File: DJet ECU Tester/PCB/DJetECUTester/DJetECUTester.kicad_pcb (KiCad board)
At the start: 2 copper layers, 93 x 79 mm, 103 parts, among them J1 ISP, J10 ECU3, J2 ECU1, J3 USB_B_Mini, J4 BREAKOUT, J5 12V IN, J6 MPS, J7 VAC, J8 INJECTORS, J9 ECU2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

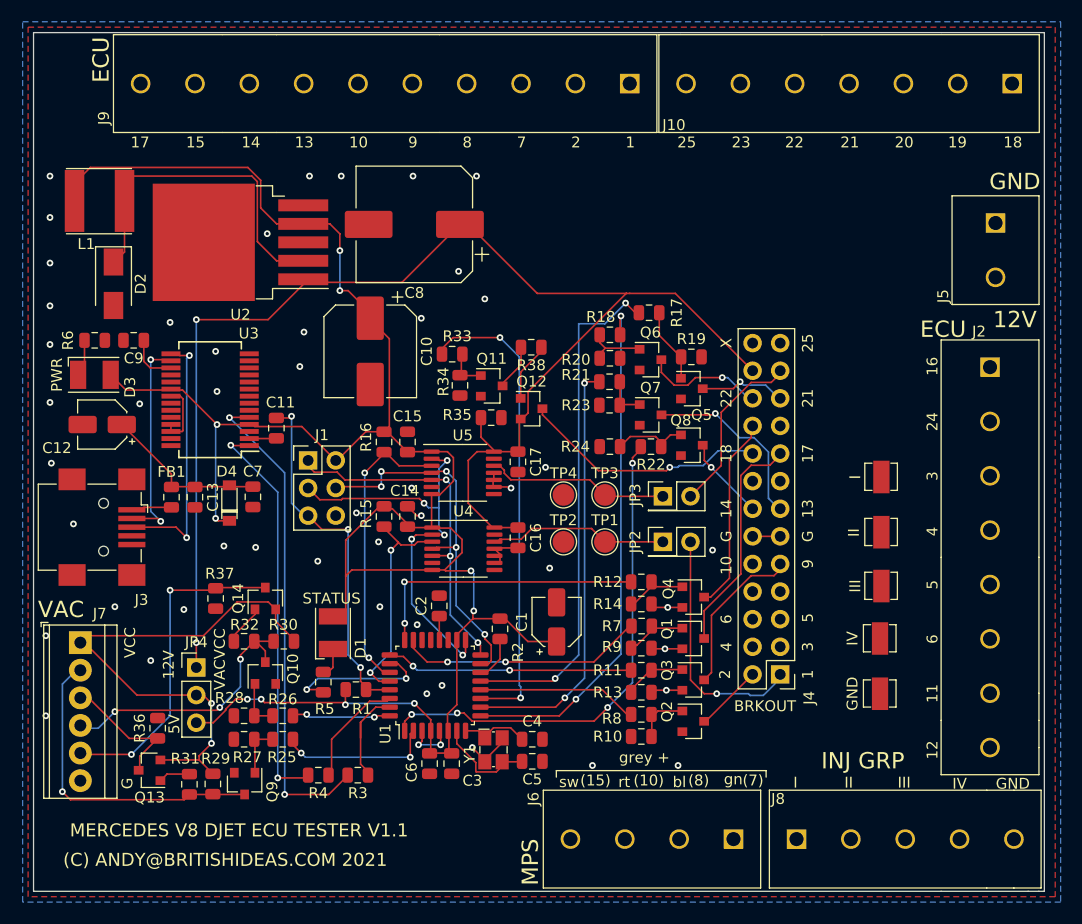
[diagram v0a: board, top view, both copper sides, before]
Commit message: Completed first attempt at new layout.
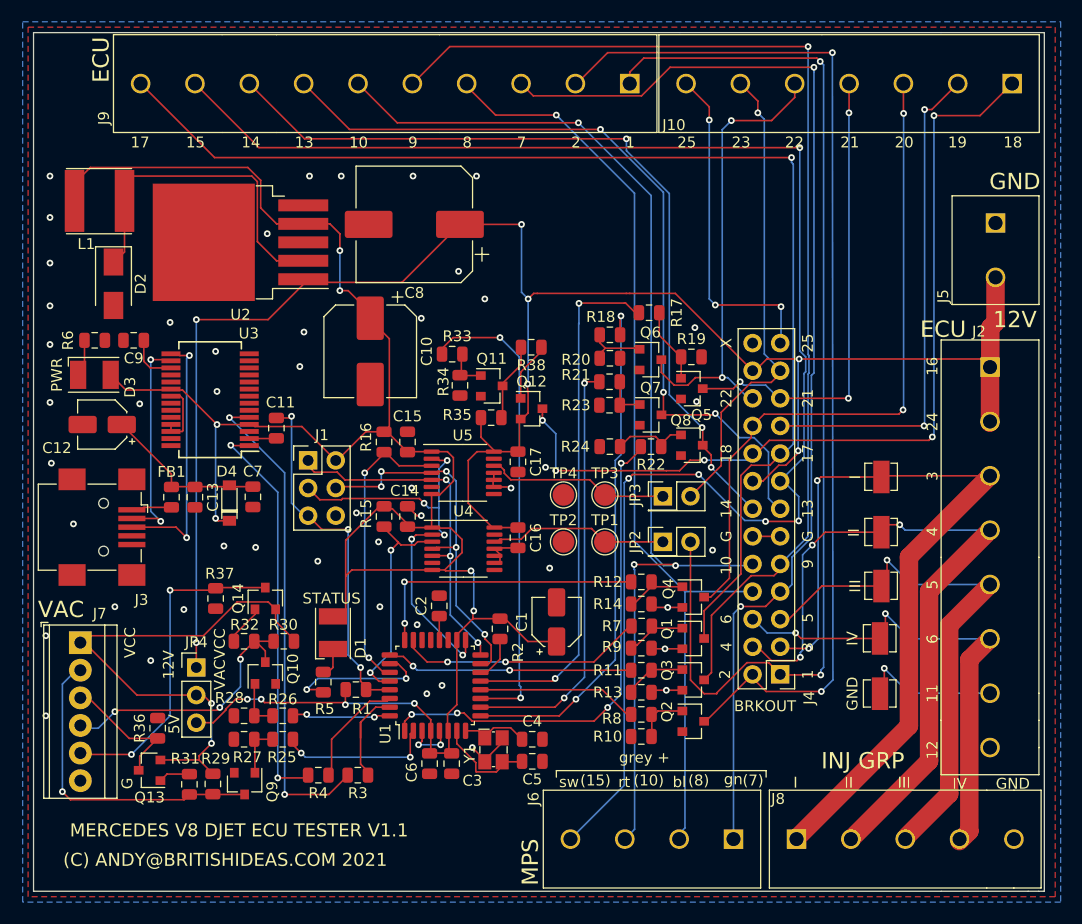
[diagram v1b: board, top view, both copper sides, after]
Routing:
- net /MPS-15: track 0.00 -> 146.9 mm, vias 0 -> 5
- net /MPS-7: track 0.00 -> 103.5 mm, vias 0 -> 2
- net /MPS-10: track 0.00 -> 103.0 mm, vias 0 -> 3
- net /ECU_TPSWOT-2: track 6.41 -> 97.1 mm, vias 0 -> 2
- net /ECU_TPSIDLE-17: track 20.6 -> 111.3 mm, vias 0 -> 1
- net /ECU_TPSACCEL1-9: track 14.1 -> 101.0 mm, vias 0 -> 1
- net /MPS-8: track 0.00 -> 86.0 mm, vias 0 -> 1
- net /ECU_AIRTEMP-1: track 21.8 -> 102.1 mm, vias 1 -> 2
- net /ECU_INJGROUP1-3: track 0.00 -> 74.7 mm, vias 0 -> 2
- net /ECU_TRIGGERGROUP4-14: track 7.43 -> 75.3 mm, vias 1 -> 3
- net /ECU_INJGROUP2-4: track 0.00 -> 66.3 mm, vias 0 -> 3
- net /ECU_TRIGGERGROUP2-13: track 16.9 -> 74.6 mm, vias 1 -> 3
- net /ECU_START-18: track 22.7 -> 79.7 mm, vias 1 -> 5
- net +12V: track 126.5 -> 177.9 mm, vias 2 -> 7
- net /ECU_INJGROUP3-5: track 0.00 -> 48.0 mm, vias 0 -> 1
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
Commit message: Added D-Jetronic text and stiching vias.
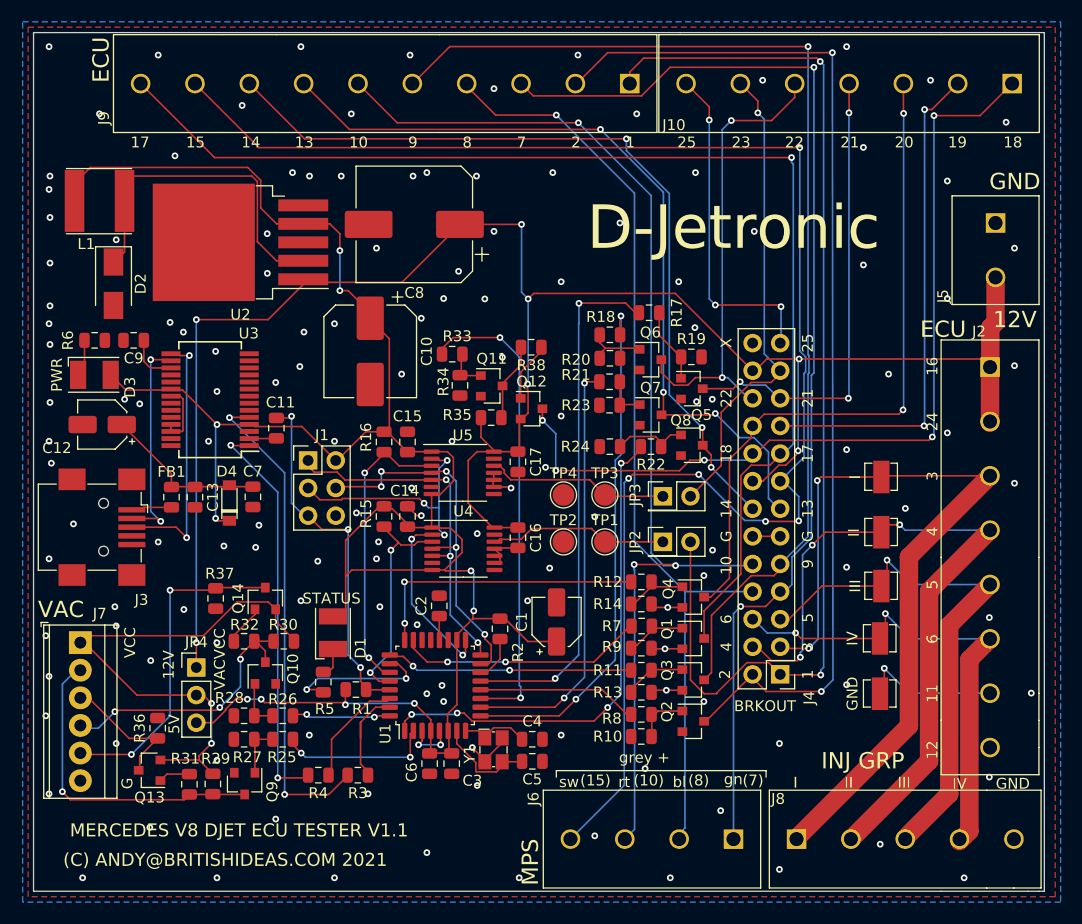
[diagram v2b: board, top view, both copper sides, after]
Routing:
- net GND: vias 51 -> 145
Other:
- board text added: "D-Jetronic"
